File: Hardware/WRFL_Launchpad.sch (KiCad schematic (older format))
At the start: 6 parts, among them P13 LAUNCHPAD_J1_J3, P14 LAUNCHPAD_J2_J4, P8 1x2_2.54_Fem, U11 REF3312

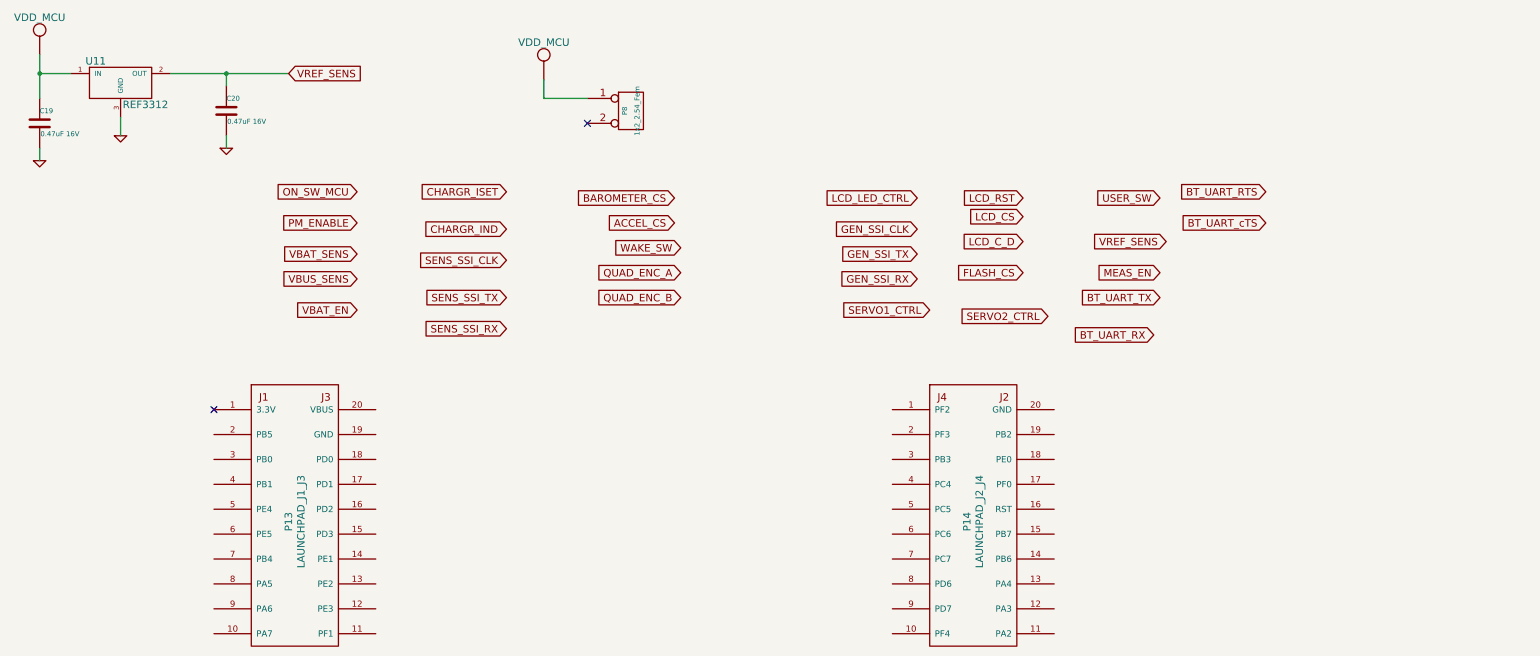
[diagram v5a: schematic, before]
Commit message: MCU function assignment
BT RTS/CTS as test points,
BT reset GPIO option
Launchpad header pin function assignment (for ERC check)
Power symbols corrections
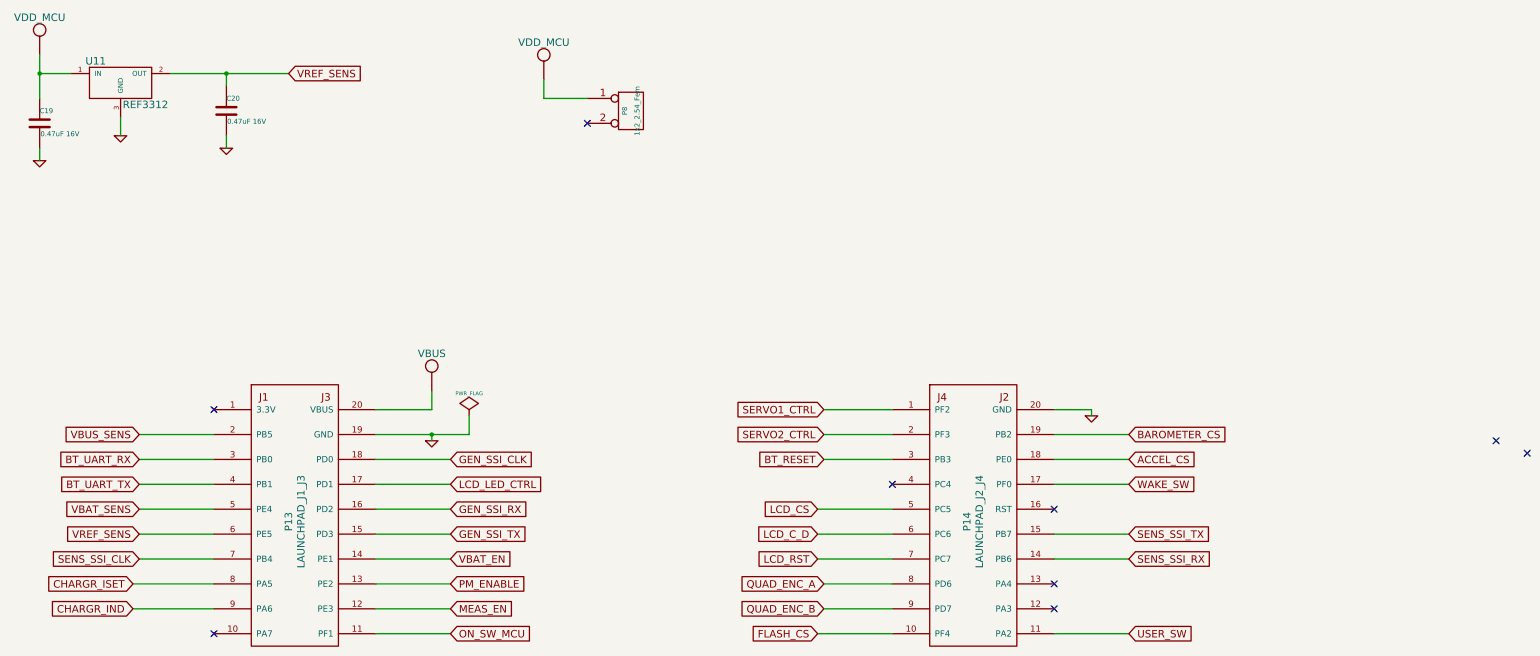
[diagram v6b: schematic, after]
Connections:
- net ACCEL_CS: now also P14.18 (PE0)
- net BAROMETER_CS: now also P14.19 (PB2)
- net BT_UART_RX: now also P13.3 (PB0)
- net BT_UART_TX: now also P13.4 (PB1)
- net CHARGR_IND: now also P13.9 (PA6)
- net CHARGR_ISET: now also P13.8 (PA5)
- net FLASH_CS: now also P14.10 (PF4)
- net GEN_SSI_CLK: now also P13.18 (PD0)
- net GEN_SSI_RX: now also P13.16 (PD2)
- net GEN_SSI_TX: now also P13.15 (PD3)
- net GND: now also P13.19 (GND), P14.20 (GND)
- net LCD_CS: now also P14.5 (PC5)
- net LCD_C_D: now also P14.6 (PC6)
- net LCD_LED_CTRL: now also P13.17 (PD1)
- net LCD_RST: now also P14.7 (PC7)
- net MEAS_EN: now also P13.12 (PE3)
- net ON_SW_MCU: now also P13.11 (PF1)
- net PM_ENABLE: now also P13.13 (PE2)
- net QUAD_ENC_A: now also P14.8 (PD6)
- net QUAD_ENC_B: now also P14.9 (PD7)
- net SENS_SSI_CLK: now also P13.7 (PB4)
- net SENS_SSI_RX: now also P14.14 (PB6)
- net SENS_SSI_TX: now also P14.15 (PB7)
- net SERVO1_CTRL: now also P14.1 (PF2)
- net SERVO2_CTRL: now also P14.2 (PF3)
- net USER_SW: now also P14.11 (PA2)
- net VBAT_EN: now also P13.14 (PE1)
- net VBAT_SENS: now also P13.5 (PE4)
- net VBUS_SENS: now also P13.2 (PB5)
- net VREF_SENS: now also P13.6 (PE5)
- net WAKE_SW: now also P14.17 (PF0)
- net VBUS: now reaches P13.20 (VBUS)
- net BT_RESET: now reaches P14.3 (PB3)
- no-connect marks 2 -> 9
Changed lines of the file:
@@
-EESchema Schematic File Version 2  date Tuesday, October 15, 2013 09:37:22 AM
+EESchema Schematic File Version 2  date Tuesday, October 22, 2013 02:02:38 PM
 LIBS:power
 LIBS:device
@@
 Sheet 3 6
 Title ""
-Date "15 oct 2013"
+Date "22 oct 2013"
 Rev ""
 Comp "Nightmechanic"
@@
 NoConn ~ 5550 1650
 $Comp
-L VDD_MCU #U12
+L VDD_MCU #U040
 U 1 1 524B47E3
 P 5200 1100
-F 0 "#U12" H 5200 1300 60  0001 C CNN
+F 0 "#U040" H 5200 1300 60  0001 C CNN
 F 1 "VDD_MCU" H 5200 1200 60  0000 C CNN
 F 2 "~" H 5200 1100 60  0000 C CNN
@@
 	1    0    0    -1
 $EndComp
-Text GLabel 3700 2200 0    60   Input ~ 0
+Text GLabel 4450 5750 2    60   Input ~ 0
 ON_SW_MCU
-Text GLabel 3700 2450 0    60   Input ~ 0
+Text GLabel 4450 5350 2    60   Input ~ 0
 PM_ENABLE
-Text GLabel 3700 2700 0    60   Input ~ 0
+Text GLabel 1950 4750 0    60   Input ~ 0
 VBAT_SENS
-Text GLabel 3700 2900 0    60   Input ~ 0
+Text GLabel 1950 4150 0    60   Input ~ 0
 VBUS_SENS
-Text GLabel 3700 3150 0    60   Input ~ 0
+Text GLabel 4450 5150 2    60   Input ~ 0
 VBAT_EN
-Text GLabel 4900 2200 0    60   Input ~ 0
+Text GLabel 1900 5350 0    60   Input ~ 0
 CHARGR_ISET
-Text GLabel 4900 2500 0    60   Input ~ 0
+Text GLabel 1900 5550 0    60   Input ~ 0
 CHARGR_IND
-Text GLabel 4900 2750 0    60   Input ~ 0
+Text GLabel 1950 5150 0    60   Input ~ 0
 SENS_SSI_CLK
-Text GLabel 4900 3050 0    60   Input ~ 0
+Text GLabel 9900 4950 2    60   Input ~ 0
 SENS_SSI_TX
-Text GLabel 4900 3300 0    60   Input ~ 0
+Text GLabel 9900 5150 2    60   Input ~ 0
 SENS_SSI_RX
-Text GLabel 6250 2250 0    60   Input ~ 0
+Text GLabel 9900 4150 2    60   Input ~ 0
 BAROMETER_CS
-Text GLabel 6250 2450 0    60   Input ~ 0
+Text GLabel 9900 4350 2    60   Input ~ 0
 ACCEL_CS
-Text GLabel 6300 2650 0    60   Input ~ 0
+Text GLabel 9900 4550 2    60   Input ~ 0
 WAKE_SW
-Text GLabel 6300 2850 0    60   Input ~ 0
+Text GLabel 7450 5350 0    60   Input ~ 0
 QUAD_ENC_A
-Text GLabel 6300 3050 0    60   Input ~ 0
+Text GLabel 7450 5550 0    60   Input ~ 0
 QUAD_ENC_B
-Text GLabel 10150 2250 0    60   Input ~ 0
+Text GLabel 9900 5750 2    60   Input ~ 0
 USER_SW
-Text GLabel 8200 2250 0    60   Input ~ 0
+Text GLabel 4450 4550 2    60   Input ~ 0
 LCD_LED_CTRL
-Text GLabel 8200 2500 0    60   Input ~ 0
+Text GLabel 4450 4350 2    60   Input ~ 0
 GEN_SSI_CLK
-Text GLabel 8200 2700 0    60   Input ~ 0
+Text GLabel 4450 4950 2    60   Input ~ 0
 GEN_SSI_TX
-Text GLabel 8200 2900 0    60   Input ~ 0
+Text GLabel 4450 4750 2    60   Input ~ 0
 GEN_SSI_RX
-Text GLabel 9050 2250 0    60   Input ~ 0
+Text GLabel 7400 5150 0    60   Input ~ 0
 LCD_RST
-Text GLabel 9050 2400 0    60   Input ~ 0
+Text GLabel 7400 4750 0    60   Input ~ 0
 LCD_CS
-Text GLabel 9050 2600 0    60   Input ~ 0
+Text GLabel 7400 4950 0    60   Input ~ 0
 LCD_C_D
-Text GLabel 9050 2850 0    60   Input ~ 0
+Text GLabel 7400 5750 0    60   Input ~ 0
 FLASH_CS
 NoConn ~ 2550 3950
-Text GLabel 8300 3150 0    60   Input ~ 0
+Text GLabel 7450 3950 0    60   Input ~ 0
 SERVO1_CTRL
-Text GLabel 9250 3200 0    60   Input ~ 0
+Text GLabel 7450 4150 0    60   Input ~ 0
 SERVO2_CTRL
-Text GLabel 10200 2600 0    60   Input ~ 0
-VREF_SENS
 $Comp
 L REF3312 U11
@@
 $EndComp
 $Comp
-L VDD_MCU #U11
+L VDD_MCU #U041
 U 1 1 525246DC
 P 1150 900
-F 0 "#U11" H 1150 1100 60  0001 C CNN
+F 0 "#U041" H 1150 1100 60  0001 C CNN
 F 1 "VDD_MCU" H 1150 1000 60  0000 C CNN
 F 2 "~" H 1150 900 60  0000 C CNN
@@
 $EndComp
 $Comp
-L GND #PWR28
-U 1 1 525246EB
-P 1150 1950
-F 0 "#PWR28" H 1150 1950 30  0001 C CNN
-F 1 "GND" H 1150 1880 30  0001 C CNN
-F 2 "" H 1150 1950 60  0000 C CNN
-F 3 "" H 1150 1950 60  0000 C CNN
-	1    1150 1950
-	1    0    0    -1
-$EndComp
-$Comp
-L GND #PWR29
+L GND #PWR042
 U 1 1 525246FA
 P 1800 1750
-F 0 "#PWR29" H 1800 1750 30  0001 C CNN
+F 0 "#PWR042" H 1800 1750 30  0001 C CNN
 F 1 "GND" H 1800 1680 30  0001 C CNN
 F 2 "" H 1800 1750 60  0000 C CNN
@@
 $EndComp
 $Comp
-L GND #PWR30
+L GND #PWR043
 U 1 1 52524709
 P 2650 1850
-F 0 "#PWR30" H 2650 1850 30  0001 C CNN
+F 0 "#PWR043" H 2650 1850 30  0001 C CNN
 F 1 "GND" H 2650 1780 30  0001 C CNN
 F 2 "" H 2650 1850 60  0000 C CNN
@@
 	1    0    0    -1
 $EndComp
-Text GLabel 10150 2850 0    60   Input ~ 0
+Text GLabel 4450 5550 2    60   Input ~ 0
 MEAS_EN
-Text GLabel 10150 3050 0    60   Input ~ 0
+Text GLabel 1950 4550 0    60   Input ~ 0
 BT_UART_TX
-Text GLabel 10100 3350 0    60   Input ~ 0
+Text GLabel 1950 4350 0    60   Input ~ 0
 BT_UART_RX
-Text GLabel 11000 2200 0    60   Input ~ 0
-BT_UART_RTS
-Text GLabel 11000 2450 0    60   Input ~ 0
-BT_UART_cTS
+Text GLabel 7450 4350 0    60   Input ~ 0
+BT_RESET
 Text GLabel 3150 1250 2    60   Input ~ 0
 VREF_SENS
 Connection ~ 2650 1250
+Text GLabel 1950 4950 0    60   Input ~ 0
+VREF_SENS
+$Comp
+L VBUS #U044
+U 1 1 526426B1
+P 4300 3600
+F 0 "#U044" H 4300 3800 60  0001 C CNN
+F 1 "VBUS" H 4300 3700 60  0000 C CNN
+F 2 "~" H 4300 3600 60  0000 C CNN
+F 3 "~" H 4300 3600 60  0000 C CNN
+	1    4300 3600
+	1    0    0    -1
+$EndComp
+NoConn ~ 9300 4750
+NoConn ~ 12850 4200
+NoConn ~ 13100 4300
+Wire Wire Line
+	2550 4150 1950 4150
+Wire Wire Line
+	1950 4350 2550 4350
+Wire Wire Line
+	2550 4550 1950 4550
+Wire Wire Line
+	1950 4750 2550 4750
+Wire Wire Line
+	2550 4950 1950 4950
+Wire Wire Line
+	1950 5150 2550 5150
+Wire Wire Line
+	4450 4350 3850 4350
+Wire Wire Line
+	4450 4550 3850 4550
+Wire Wire Line
+	4450 4750 3850 4750
+Wire Wire Line
+	4450 4950 3850 4950
+Wire Wire Line
+	3850 3950 4300 3950
+Wire Wire Line
+	4300 3950 4300 3800
+$Comp
+L GND #PWR045
+U 1 1 52642A59
+P 4300 4200
+F 0 "#PWR045" H 4300 4200 30  0001 C CNN
+F 1 "GND" H 4300 4130 30  0001 C CNN
+F 2 "" H 4300 4200 60  0000 C CNN
+F 3 "" H 4300 4200 60  0000 C CNN
+	1    4300 4200
+	1    0    0    -1
+$EndComp
+Wire Wire Line
+	3850 4150 4600 4150
+Wire Wire Line
+	4300 4150 4300 4200
+Wire Wire Line
+	8000 3950 7450 3950
+Wire Wire Line
+	7450 4150 8000 4150
+Wire Wire Line
+	8000 5350 7450 5350
+Wire Wire Line
+	8000 5550 7450 5550
+Wire Wire Line
+	9300 4550 9900 4550
+Wire Wire Line
+	9300 4950 9900 4950
+Wire Wire Line
+	9900 5150 9300 5150
+$Comp
+L GND #PWR046
+U 1 1 52642B7B
+P 9600 4000
+F 0 "#PWR046" H 9600 4000 30  0001 C CNN
+F 1 "GND" H 9600 3930 30  0001 C CNN
+F 2 "" H 9600 4000 60  0000 C CNN
+F 3 "" H 9600 4000 60  0000 C CNN
+	1    9600 4000
+	1    0    0    -1
+$EndComp
+Wire Wire Line
+	9300 3950 9600 3950
+Wire Wire Line
+	9600 3950 9600 4000
+Wire Wire Line
+	2550 5350 1900 5350
+Wire Wire Line
+	2550 5550 1900 5550
+Wire Wire Line
+	3850 5150 4450 5150
+Wire Wire Line
+	4450 5350 3850 5350
+Wire Wire Line
+	3850 5550 4450 5550
+Wire Wire Line
+	4450 5750 3850 5750
+Wire Wire Line
+	9900 4150 9300 4150
+Wire Wire Line
+	9300 4350 9900 4350
+Wire Wire Line
+	8000 5150 7400 5150
+Wire Wire Line
+	8000 4950 7400 4950
+Wire Wire Line
+	7400 4750 8000 4750
+Wire Wire Line
+	8000 5750 7400 5750
+Wire Wire Line
+	8000 4350 7450 4350
+NoConn ~ 9300 5350
+NoConn ~ 9300 5550
+NoConn ~ 8000 4550
+NoConn ~ 2550 5750
+Wire Wire Line
+	9900 5750 9300 5750
+$Comp
+L GND #PWR047
+U 1 1 52664487
+P 1150 1950
+F 0 "#PWR047" H 1150 1950 30  0001 C CNN
+F 1 "GND" H 1150 1880 30  0001 C CNN
+F 2 "" H 1150 1950 60  0000 C CNN
+F 3 "" H 1150 1950 60  0000 C CNN
+	1    1150 1950
+	1    0    0    -1
+$EndComp
+$Comp
+L PWR_FLAG #FLG048
+U 1 1 52665EE1
+P 4600 4000
+F 0 "#FLG048" H 4600 4095 30  0001 C CNN
+F 1 "PWR_FLAG" H 4600 4180 30  0000 C CNN
+F 2 "" H 4600 4000 60  0000 C CNN
+F 3 "" H 4600 4000 60  0000 C CNN
+	1    4600 4000
+	1    0    0    -1
+$EndComp
+Wire Wire Line
+	4600 4150 4600 4000
+Connection ~ 4300 4150
 $EndSCHEMATC

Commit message: Added BAT temp sens
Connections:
- net MEAS_EN: now also P13.10 (PA7); no longer P13.12 (PE3)
- new net BAT_TEMP_SENS: P13.12 (PE3)
- no-connect marks 9 -> 8
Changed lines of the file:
@@
-EESchema Schematic File Version 2  date Tuesday, October 22, 2013 02:02:38 PM
+EESchema Schematic File Version 2  date Sunday, October 27, 2013 'AMt' 10:59:49 AM
 LIBS:power
 LIBS:device
@@
 Sheet 3 6
 Title ""
-Date "22 oct 2013"
+Date "27 oct 2013"
 Rev ""
 Comp "Nightmechanic"
@@
 NoConn ~ 5550 1650
 $Comp
-L VDD_MCU #U040
+L VDD_MCU #U13
 U 1 1 524B47E3
 P 5200 1100
-F 0 "#U040" H 5200 1300 60  0001 C CNN
+F 0 "#U13" H 5200 1300 60  0001 C CNN
 F 1 "VDD_MCU" H 5200 1200 60  0000 C CNN
 F 2 "~" H 5200 1100 60  0000 C CNN
@@
 $EndComp
 $Comp
-L VDD_MCU #U041
+L VDD_MCU #U11
 U 1 1 525246DC
 P 1150 900
-F 0 "#U041" H 1150 1100 60  0001 C CNN
+F 0 "#U11" H 1150 1100 60  0001 C CNN
 F 1 "VDD_MCU" H 1150 1000 60  0000 C CNN
 F 2 "~" H 1150 900 60  0000 C CNN
@@
 $EndComp
 $Comp
-L GND #PWR042
+L GND #PWR29
 U 1 1 525246FA
 P 1800 1750
-F 0 "#PWR042" H 1800 1750 30  0001 C CNN
+F 0 "#PWR29" H 1800 1750 30  0001 C CNN
 F 1 "GND" H 1800 1680 30  0001 C CNN
 F 2 "" H 1800 1750 60  0000 C CNN
@@
 $EndComp
 $Comp
-L GND #PWR043
+L GND #PWR30
 U 1 1 52524709
 P 2650 1850
-F 0 "#PWR043" H 2650 1850 30  0001 C CNN
+F 0 "#PWR30" H 2650 1850 30  0001 C CNN
 F 1 "GND" H 2650 1780 30  0001 C CNN
 F 2 "" H 2650 1850 60  0000 C CNN
@@
 $EndComp
 Wire Wire Line
-	1150 1100 1150 1450
+	1150 1100 1150 1250
+Wire Wire Line
+	1150 1250 1150 1450
 Wire Wire Line
 	1150 1850 1150 1950
@@
 	1800 1600 1800 1750
 Wire Wire Line
-	2200 1250 3150 1250
+	2200 1250 2650 1250
+Wire Wire Line
+	2650 1250 3150 1250
 Wire Wire Line
 	2650 1250 2650 1350
@@
 	1    0    0    -1
 $EndComp
-Text GLabel 4450 5550 2    60   Input ~ 0
+Text GLabel 1900 5750 0    60   Input ~ 0
 MEAS_EN
 Text GLabel 1950 4550 0    60   Input ~ 0
@@
 VREF_SENS
 $Comp
-L VBUS #U044
+L VBUS #U12
 U 1 1 526426B1
 P 4300 3600
-F 0 "#U044" H 4300 3800 60  0001 C CNN
+F 0 "#U12" H 4300 3800 60  0001 C CNN
 F 1 "VBUS" H 4300 3700 60  0000 C CNN
 F 2 "~" H 4300 3600 60  0000 C CNN
@@
 	4300 3950 4300 3800
 $Comp
-L GND #PWR045
+L GND #PWR31
 U 1 1 52642A59
 P 4300 4200
-F 0 "#PWR045" H 4300 4200 30  0001 C CNN
+F 0 "#PWR31" H 4300 4200 30  0001 C CNN
 F 1 "GND" H 4300 4130 30  0001 C CNN
 F 2 "" H 4300 4200 60  0000 C CNN
@@
 $EndComp
 Wire Wire Line
-	3850 4150 4600 4150
+	3850 4150 4300 4150
+Wire Wire Line
+	4300 4150 4600 4150
 Wire Wire Line
 	4300 4150 4300 4200
@@
 	9900 5150 9300 5150
 $Comp
-L GND #PWR046
+L GND #PWR32
 U 1 1 52642B7B
 P 9600 4000
-F 0 "#PWR046" H 9600 4000 30  0001 C CNN
+F 0 "#PWR32" H 9600 4000 30  0001 C CNN
 F 1 "GND" H 9600 3930 30  0001 C CNN
 F 2 "" H 9600 4000 60  0000 C CNN
@@
 	4450 5350 3850 5350
 Wire Wire Line
-	3850 5550 4450 5550
-Wire Wire Line
 	4450 5750 3850 5750
 Wire Wire Line
@@
 NoConn ~ 9300 5550
 NoConn ~ 8000 4550
-NoConn ~ 2550 5750
 Wire Wire Line
 	9900 5750 9300 5750
 $Comp
-L GND #PWR047
+L GND #PWR28
 U 1 1 52664487
 P 1150 1950
-F 0 "#PWR047" H 1150 1950 30  0001 C CNN
+F 0 "#PWR28" H 1150 1950 30  0001 C CNN
 F 1 "GND" H 1150 1880 30  0001 C CNN
 F 2 "" H 1150 1950 60  0000 C CNN
@@
 $EndComp
 $Comp
-L PWR_FLAG #FLG048
+L PWR_FLAG #FLG3
 U 1 1 52665EE1
 P 4600 4000
-F 0 "#FLG048" H 4600 4095 30  0001 C CNN
+F 0 "#FLG3" H 4600 4095 30  0001 C CNN
 F 1 "PWR_FLAG" H 4600 4180 30  0000 C CNN
 F 2 "" H 4600 4000 60  0000 C CNN
@@
 	4600 4150 4600 4000
 Connection ~ 4300 4150
+Wire Wire Line
+	3850 5550 4450 5550
+Text GLabel 4450 5550 2    60   Input ~ 0
+BAT_TEMP_SENS
+Wire Wire Line
+	2550 5750 1900 5750
 $EndSCHEMATC
